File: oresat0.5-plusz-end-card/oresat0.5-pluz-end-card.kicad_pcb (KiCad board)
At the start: 4 copper layers, 99.8 x 94.6 mm, 30 parts, among them J1 J-SAMTEC-TFM-120-01-L-D-RA, J2 Harwin M55-7101242R, J3 Harwin M55-7101242R, J4 Harwin M55-7101242R, J5 Harwin M55-7101242R, J6 Conn_Coaxial

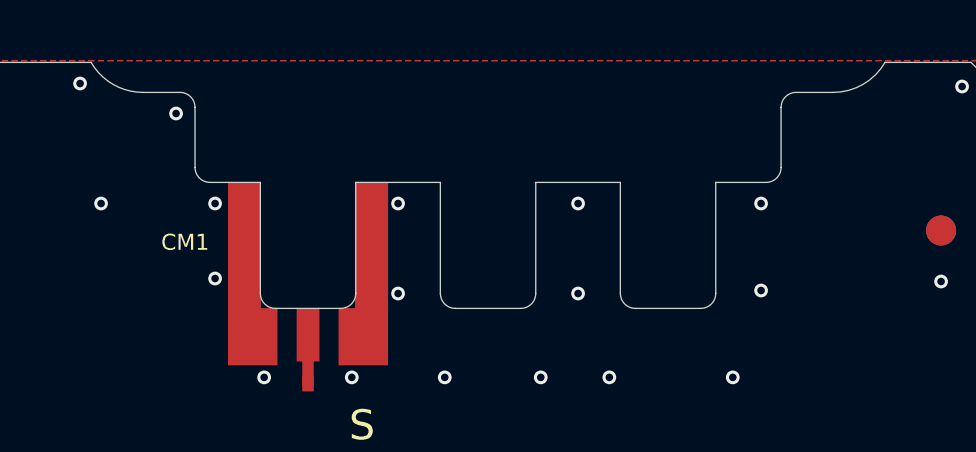
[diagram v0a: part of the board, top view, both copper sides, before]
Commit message: Updated -Z end card and replaced eagle imported libraries with kicad libraries
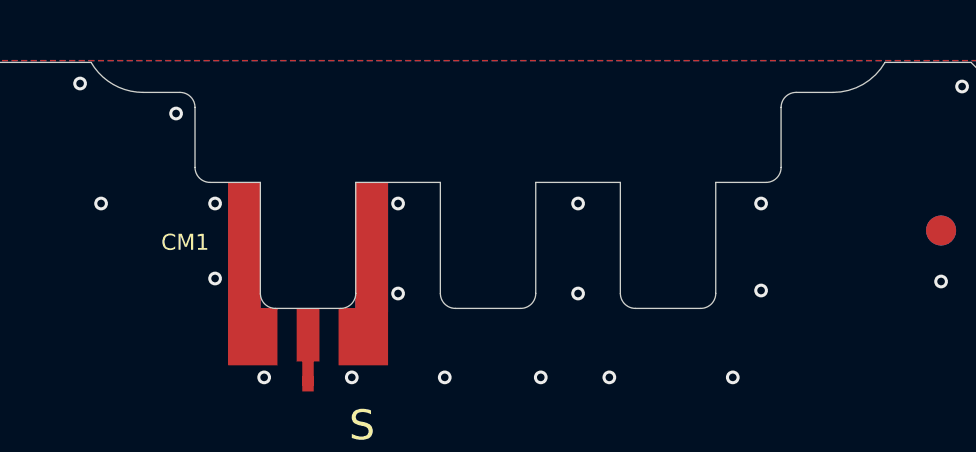
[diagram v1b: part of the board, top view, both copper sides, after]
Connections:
- J2 pad 7: /-X_AUX -> /-Y_AUX
- J2 pad 8: /-X_AUX -> /-Y_AUX
- J3 pad 7: /+Y_AUX -> /+X_AUX
- J3 pad 8: /+Y_AUX -> /+X_AUX
- J4 pad 7: /+X_AUX -> /+Y_AUX
- J4 pad 8: /+X_AUX -> /+Y_AUX
- J5 pad 7: /-Y_AUX -> /-X_AUX
- J5 pad 8: /-Y_AUX -> /-X_AUX
- TP5 pad 1: /-X_AUX -> /-Y_AUX
- TP6 pad 1: /+Y_AUX -> /+X_AUX
- TP7 pad 1: /+X_AUX -> /+Y_AUX
- TP8 pad 1: /-Y_AUX -> /-X_AUX
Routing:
- net /+Y_AUX: track 7.33 -> 3.28 mm
- net /+X_AUX: track 3.28 -> 7.33 mm

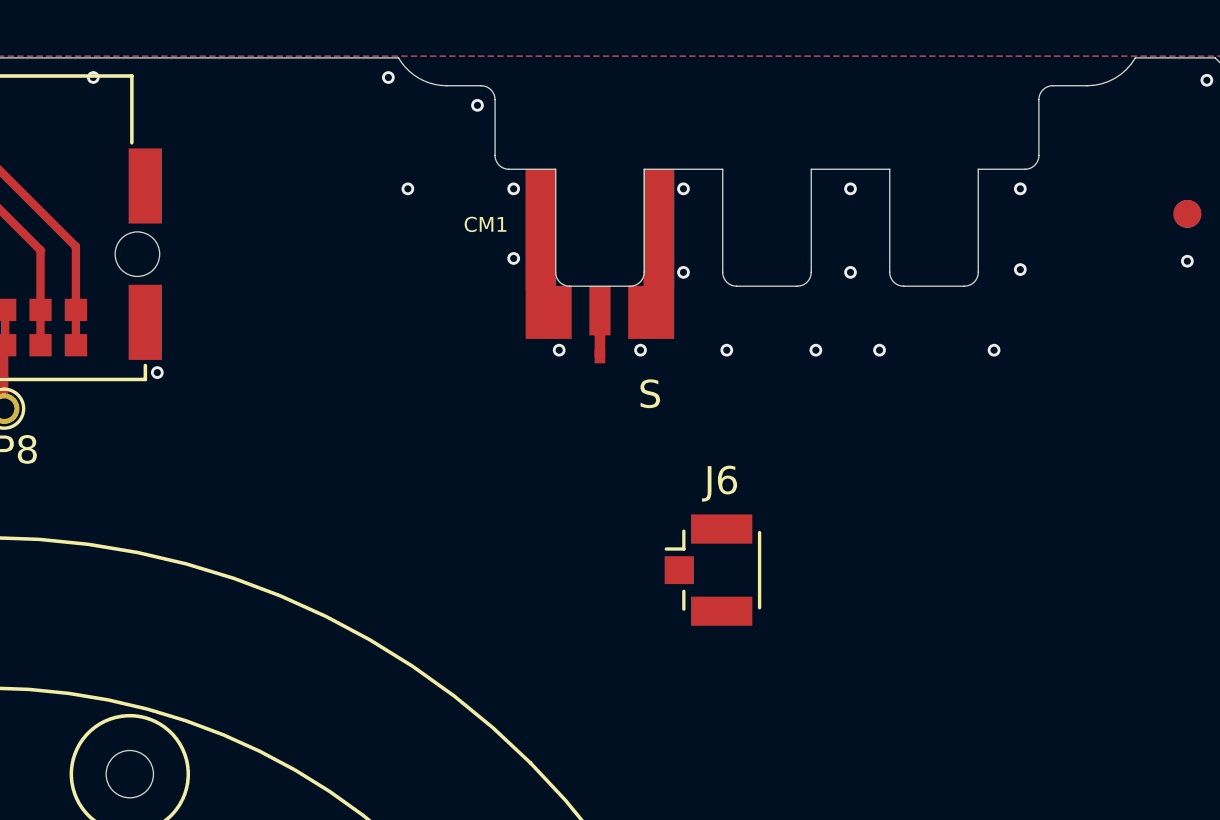
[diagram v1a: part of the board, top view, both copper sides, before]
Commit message: Added helical landing pad and left hopefully enough room for Garrett to put in matching components.
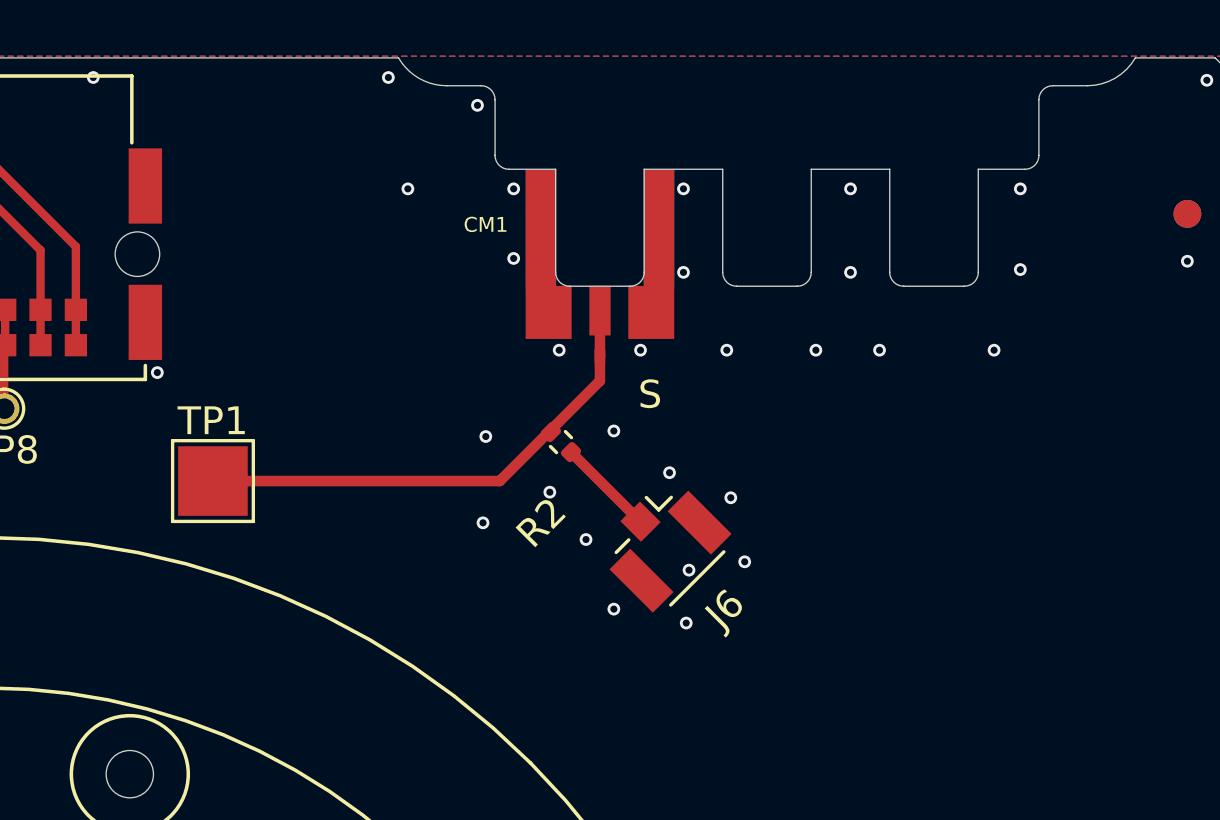
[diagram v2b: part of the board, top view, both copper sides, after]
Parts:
- added R2: NP, Resistor_SMD:R_0402_1005Metric, F.Cu at (169.1, 71.5)
- added TP1: Helical Landing Patch on PCB, TestPoint:TestPoint_Pad_2.5x2.5mm, F.Cu at (156.6, 72.9)
- moved J6 1.97 mm to (172.7, 75.1), turned to -45 degrees
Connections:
- J6 pad 1: /S BAND -> /S BAND U FL
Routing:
- net /S BAND: track 0.00 -> 16.3 mm
- net /S BAND U FL: track 0.00 -> 3.53 mm
- net GND: vias 111 -> 122

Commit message: added Matching Components
Added matching components for s band antenna, ground stitching
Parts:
- added C1: 1p, Capacitor_SMD:C_0402_1005Metric, F.Cu at (164.6, 72.9)
- added L1: 6.8n, Inductor_SMD:L_0402_1005Metric, F.Cu at (161.9, 73.4)
- moved TP1 2.93 mm to (159.5, 72.9)
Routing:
- net /S BAND: track 16.3 -> 12.4 mm, vias 0 -> 2
- net GND: track 14.2 -> 15.2 mm, vias 122 -> 137

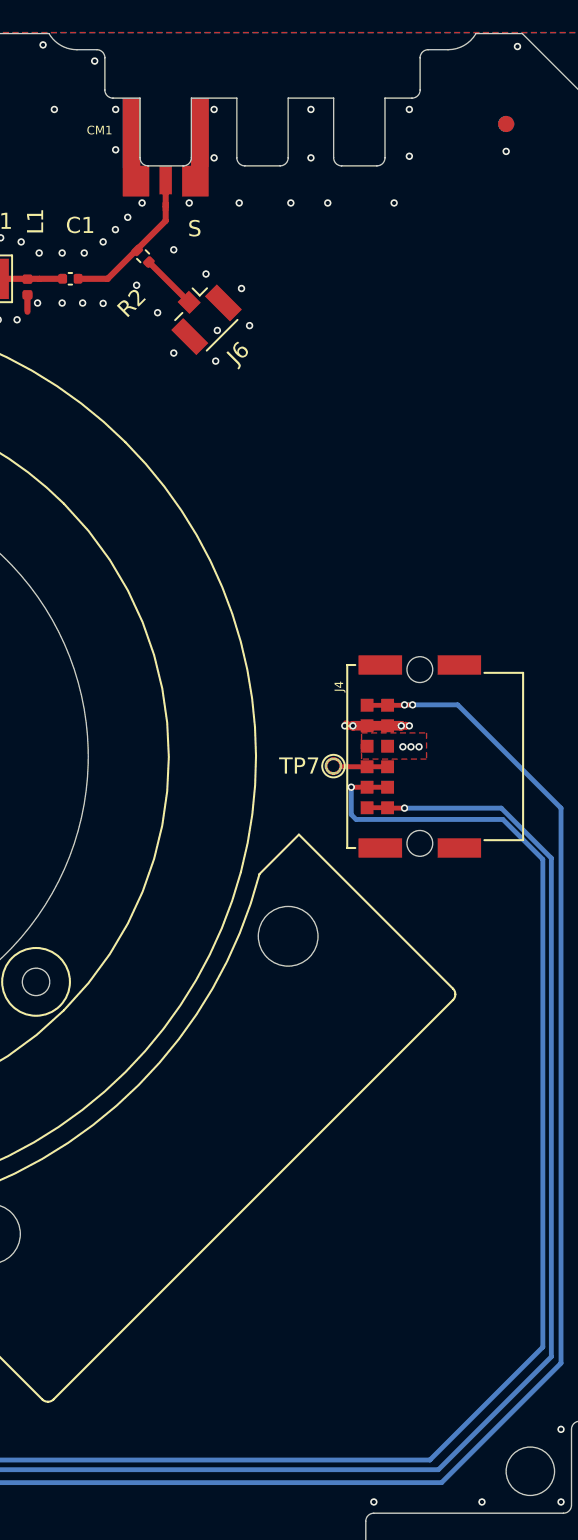
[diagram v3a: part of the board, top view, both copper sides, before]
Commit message: CAM file changes for end card PCBs.
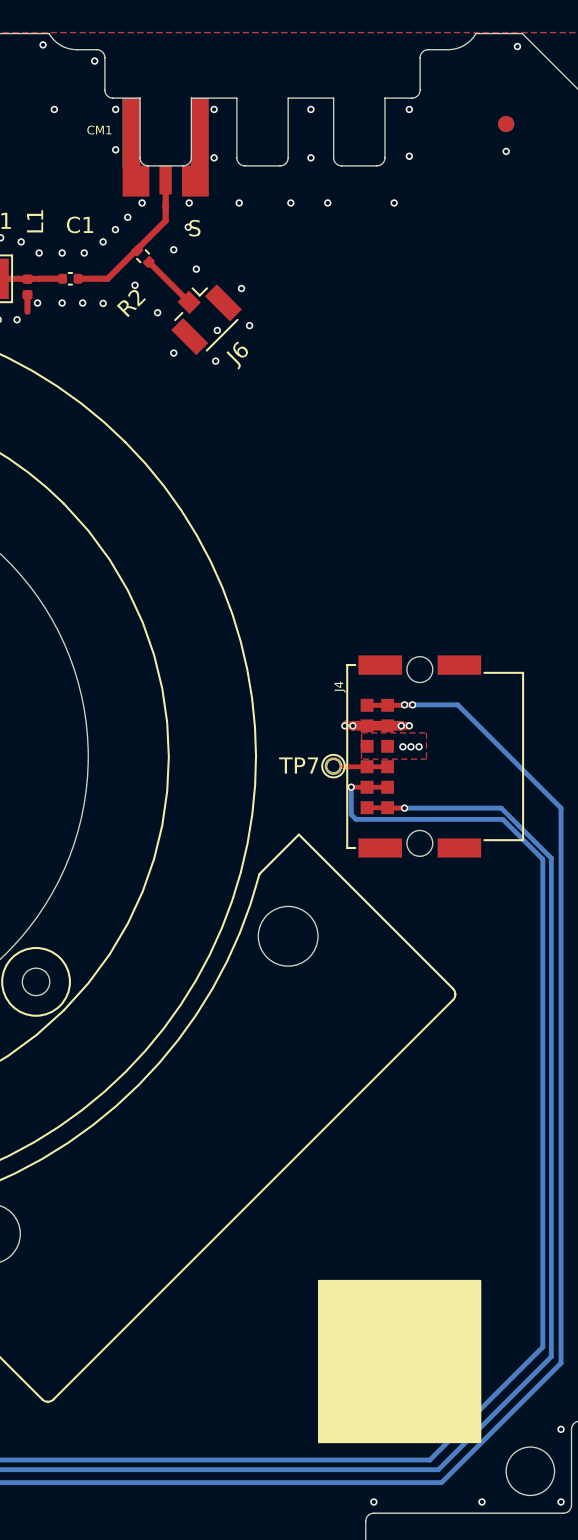
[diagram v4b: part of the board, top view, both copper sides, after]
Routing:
- net GND: vias 137 -> 140
- net /S BAND: vias 2 -> 0

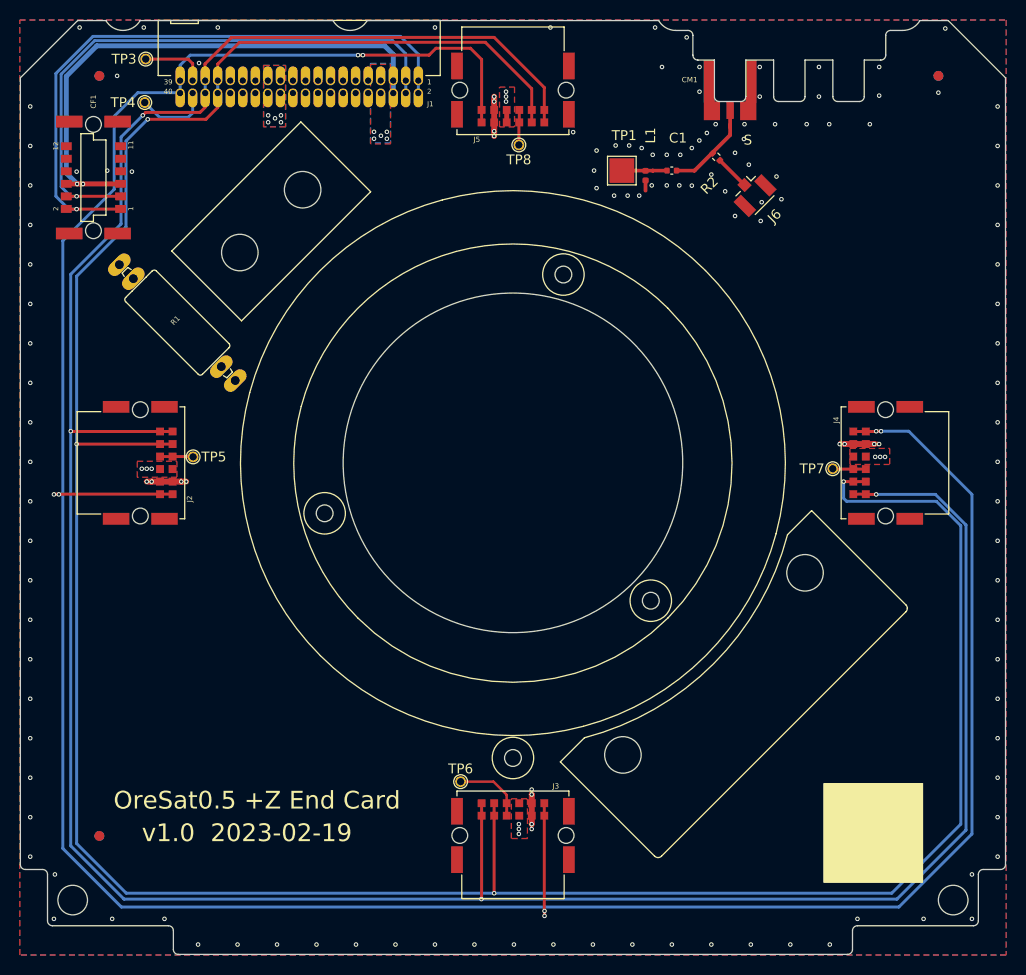
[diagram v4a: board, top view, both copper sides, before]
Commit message: Updated OreSat 0.5 end card board outlines and mounting holes, and fixed KiCad library warnings
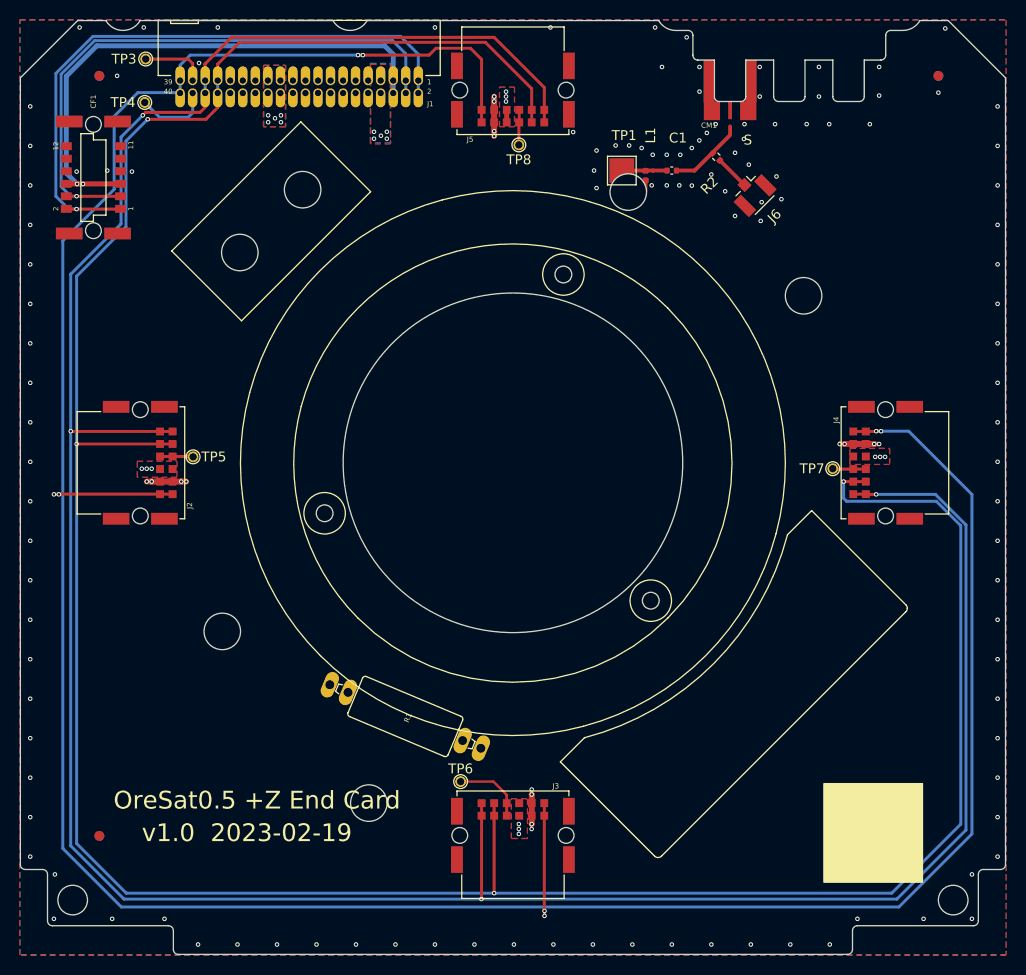
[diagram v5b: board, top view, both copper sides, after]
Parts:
- removed HW7: M1.6_Mounting_Hole, oresat-misc:M1.6 Mounting Hole
- added HW13: M2-Press-Fit-Nut, oresat-misc:M2-Press-Fit-Nut, F.Cu at (160.2, 75.1)
- added HW14: M2-Press-Fit-Nut, oresat-misc:M2-Press-Fit-Nut, F.Cu at (177.9, 85.6)
- C1: value 1p -> C
- CM1: footprint oresat-connectors:J-MOLEX-SMPM-073300-003X -> oresat-connectors:J-MOLEX-SMPM-073300-002X
- L1: value 6.8n -> L
- PCB1: footprint plusz-end-card-with-turnstile:ORESAT-CARD-V1.3-GENERIC-3RF -> oresat-pcbs:ORESAT-CARD-V1.3-3RF
- moved PCB1 70.5 mm to (148.5, 102.5)
- moved HW11 50.0 mm to (133.9, 137.0)
- moved R1 46.1 mm to (137.6, 128.2), turned to -112.8 degrees
- moved HW10 42.5 mm to (119.1, 119.6)
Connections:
- C1 pad 2: /S BAND -> Net-(C1-Pad2)
- L1 pad 1: /S BAND -> Net-(C1-Pad2)
- TP1 pad 1: /S BAND -> Net-(C1-Pad2)
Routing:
- net /S BAND: track 12.4 -> 7.80 mm
- net Net-(C1-Pad2): track 0.00 -> 4.63 mm

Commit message: Updated +Z end card
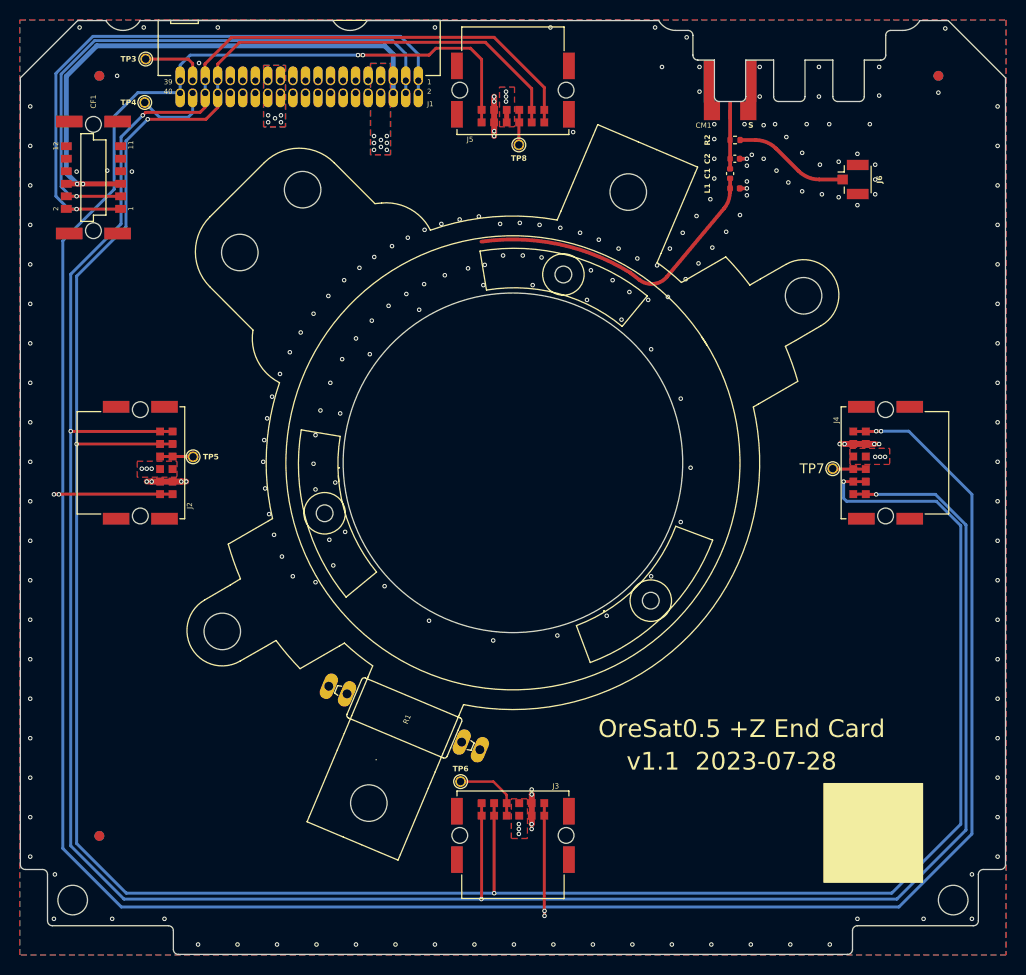
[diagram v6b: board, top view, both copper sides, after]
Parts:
- removed TP1: Helical Landing Patch on PCB, TestPoint:TestPoint_Pad_2.5x2.5mm
- added C2: NP, Capacitor_SMD:C_0402_1005Metric, F.Cu at (171.0, 71.7)
- TP3, TP4, TP5, TP6, TP7, TP8: footprint oresat-misc:TestPoint-MinTH -> oresat-misc:TestPoint-0.75mm-th
- moved J6 10.3 mm to (182.9, 73.8), turned to 0 degrees
- moved L1 9.14 mm to (171.0, 74.7), turned to 0 degrees
- moved C1 5.92 mm to (170.5, 73.2), turned to -90 degrees
- moved R2 2.55 mm to (171.0, 69.8), turned to 0 degrees
- moved R1 0.18 mm to (137.5, 128.3)
- renumbered HW8 to HW7
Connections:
- net /S BAND renamed /S_BAND
- net /S BAND U FL renamed /S_BAND_U_FL
- net Net-(C1-Pad2) renamed /S_BAND_FEED
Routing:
- net /S_BAND_FEED: track 4.63 -> 32.1 mm
- net /S_BAND_U_FL: track 3.53 -> 11.8 mm
- net /S_BAND: track 7.80 -> 5.93 mm
- net GND: track 15.2 -> 15.6 mm, vias 140 -> 221
- net /HELICAL-DEPLOY: vias 5 -> 8
- added copper zone on In2.Cu, net /HELICAL-DEPLOY
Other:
- board text added: "v1.1 2023-07-28"
- board text removed: "v1.0 2023-02-19"

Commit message: Updated mounting hole on +Z end card
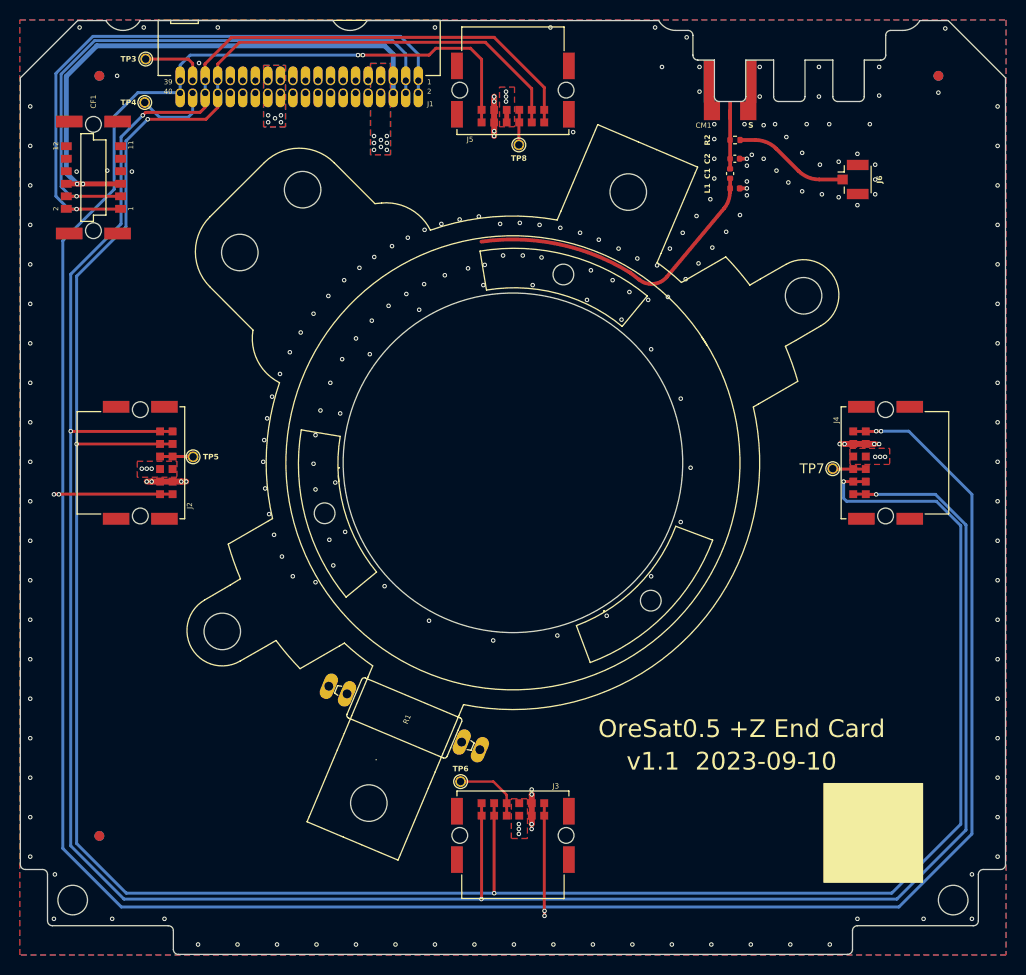
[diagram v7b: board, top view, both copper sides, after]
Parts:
- HW5, HW6, HW7: footprint oresat-misc:M1.6 Mounting Hole -> oresat-misc:Hole-2.1mm-NPTH
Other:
- board text added: "v1.1 2023-09-10"
- board text removed: "v1.1 2023-07-28"
